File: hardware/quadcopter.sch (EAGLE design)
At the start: 60 parts, among them J1 AVR_SPI_PRG_6NS, J2 HEADER-4POS-2X2-0.1IN-FEMALE-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, J3 HEADER-10POSTH-254X10, J4 HEADER-4POS-2X2-0.1IN-FEMALE-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, Q3 MOSFET-FET-SI2302CDS-T1-E3CT-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, Q4 MOSFET-FET-SI2302CDS-T1-E3CT-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, Q5 MOSFET-FET-SI2302CDS-T1-E3CT-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, Q6 MOSFET-FET-SI2302CDS-T1-E3CT-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, U1 ATMEGA128RFA1, U2 IMU-LSM6DSOXTR-497-18367-1-ND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

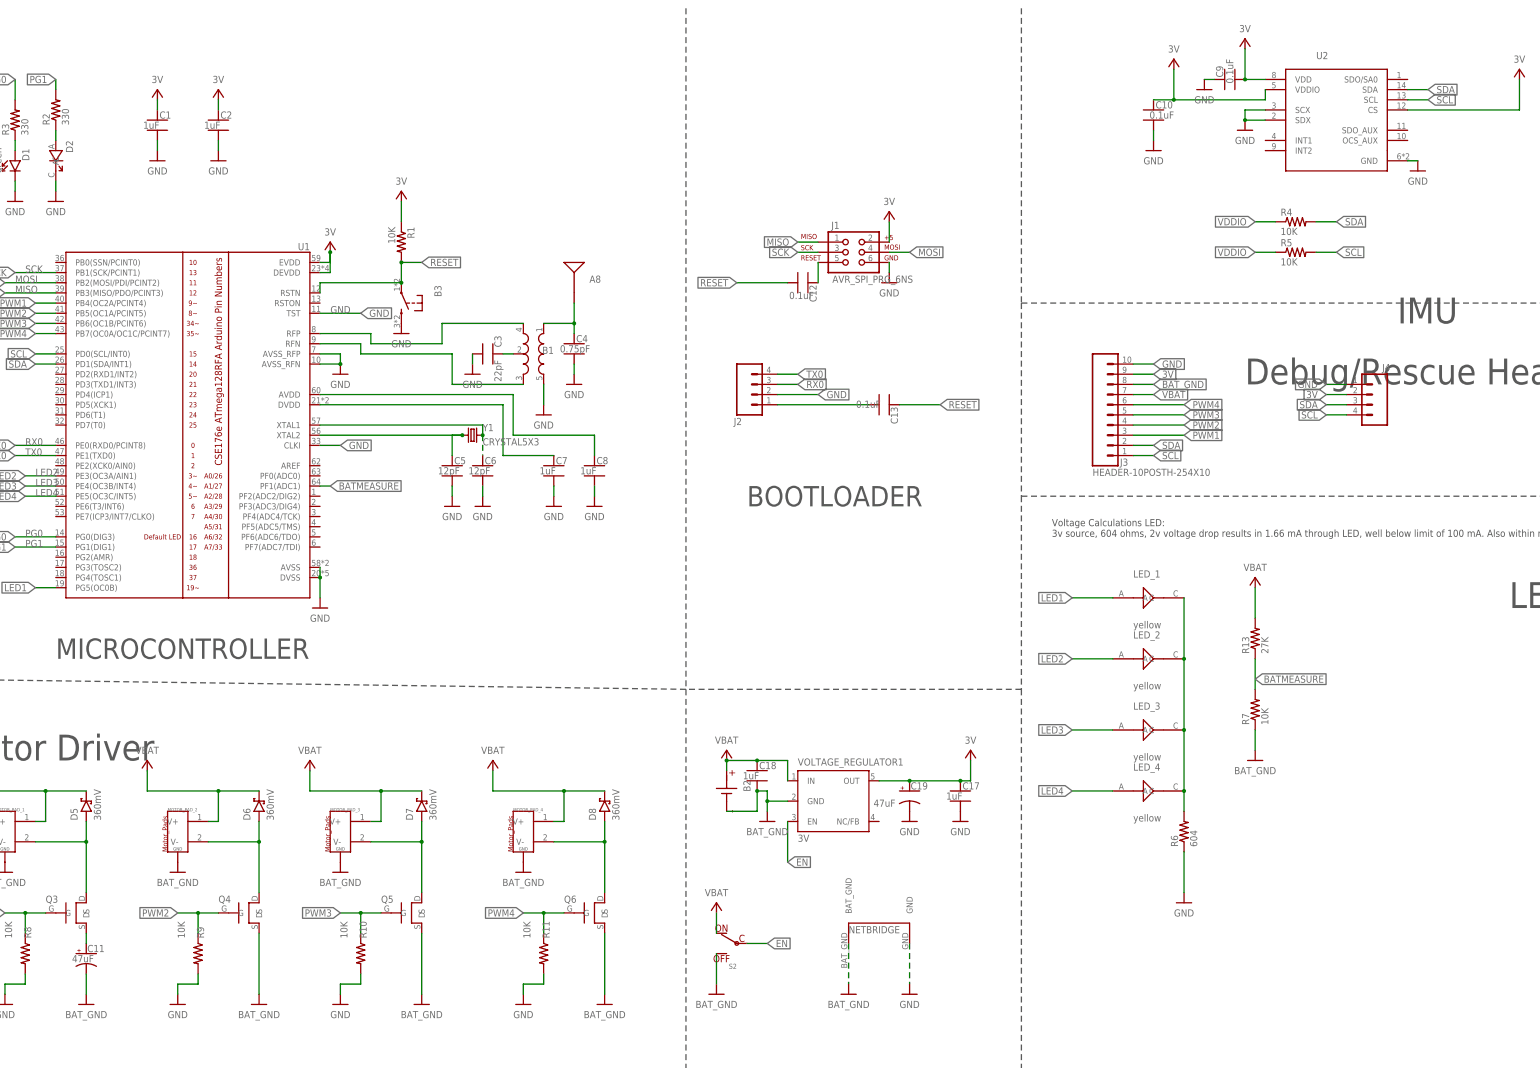
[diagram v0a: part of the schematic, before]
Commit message: fixing quadcopter schematic
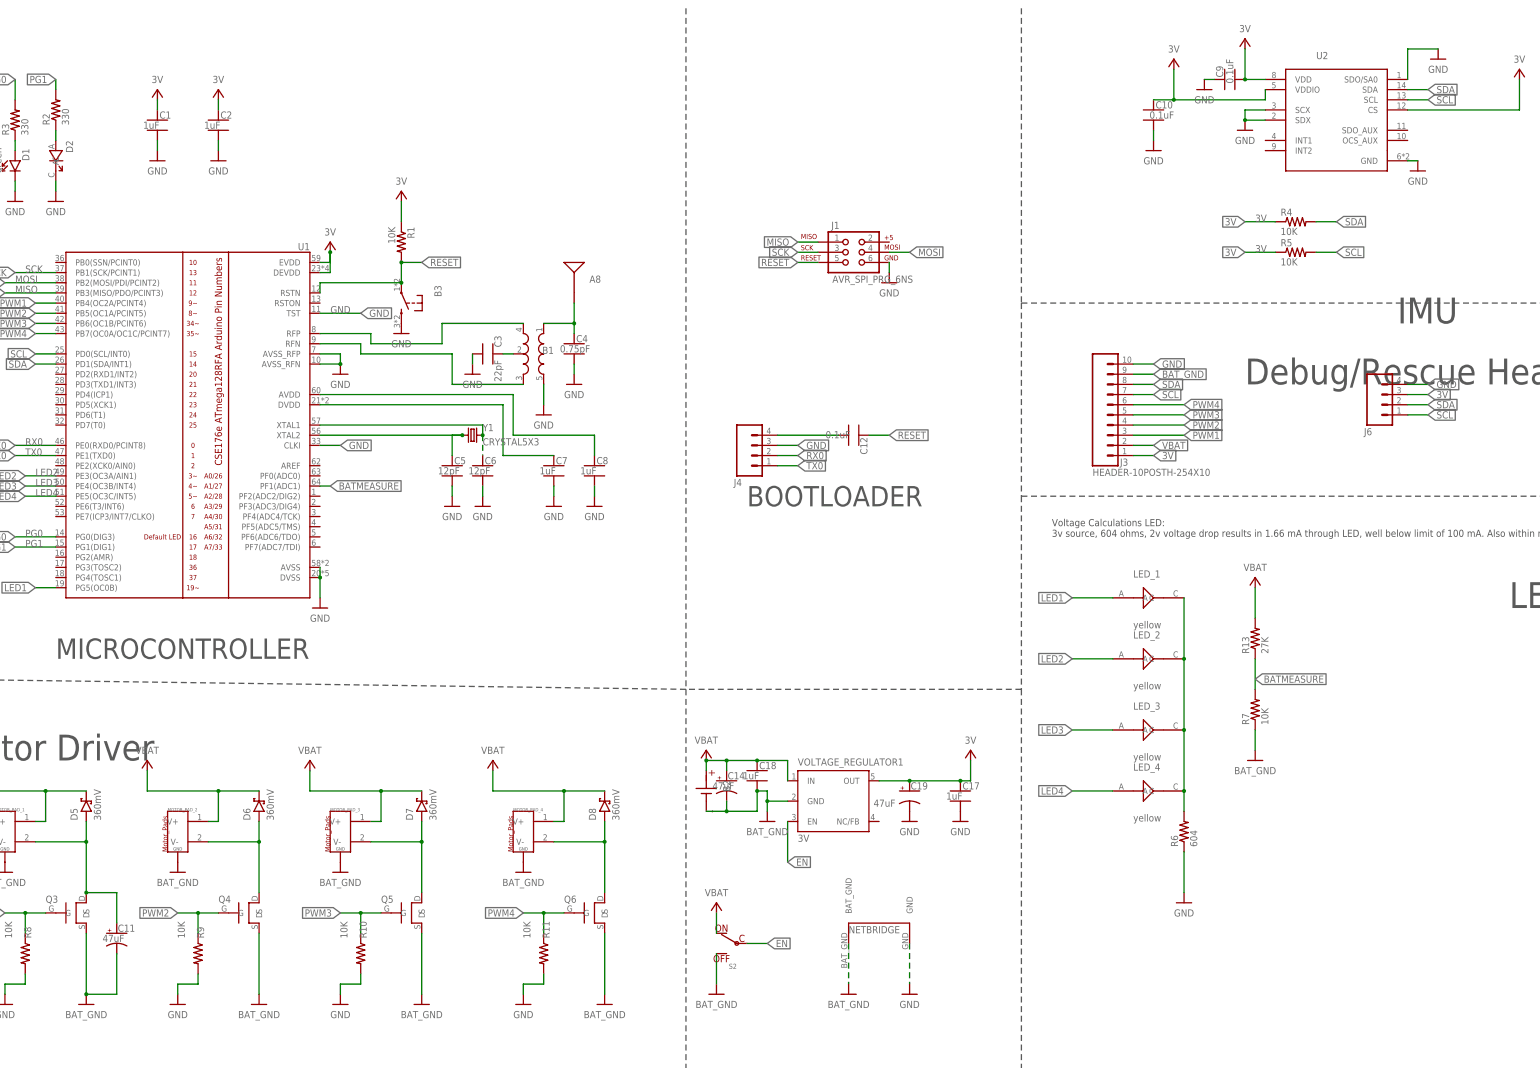
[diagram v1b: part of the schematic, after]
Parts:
- removed C13: 0.1uF, quadparts_prebuilt_2022:CAPACITOR-NP_SMD-2012-0805_CERAMIC-0.1UF
- removed J2: HEADER-4POS-2X2-0.1IN-FEMALE-SMD-BOTTOM-ENTRY, quadparts_prebuilt_2022:HEADER-4POS-2X2-0.1IN-FEMALE-SMD-BOTTOM-ENTRY
- added C14: 47uF, quadparts_prebuilt_2022:CAPACITOR-POL_47UF-SMD-1206-TAJA
- added J6: HEADER-4POS-0.1IN-FEMALE, quadparts_prebuilt_2022:HEADER-4POS-0.1IN-FEMALE
- J4: value HEADER-4POS-2X2-0.1IN-FEMALE-SMD-BOTTOM-ENTRY -> HEADER-4POS-0.1IN-FEMALE-SMD-BOTTOM-ENTRY; device quadparts_prebuilt_2022:HEADER-4POS-2X2-0.1IN-FEMALE-SMD-BOTTOM-ENTRY -> quadparts_prebuilt_2022:HEADER-4POS-0.1IN-FEMALE-SMD-BOTTOM-ENTRY
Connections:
- removed net N$15: C13.2, J2.1
- removed net N$16: C11.+, Q3.S
- removed net VDDIO: R4.1, R5.1
- net 3V: now also J3.1, J6.3, R4.1, R5.1; no longer J1.2, J3.9, J4.2
- net BAT_GND: now also C14.-, J3.9, Q3.S; no longer J3.8
- net GND: now also J4.3, J6.4, U2.SDO/SA0; no longer J2.2, J4.1
- net N$13: now also C12.2, J4.4; no longer C12.1, J1.5
- net N$18: now also C11.+
- net RESET: now also C12.1, J1.5; no longer C12.2, C13.1
- net RX0: now also J4.2; no longer J2.3
- net SCL: now also J3.7, J6.1; no longer J3.1, J4.4
- net SDA: now also J3.8, J6.2; no longer J3.2, J4.3
- net TX0: now also J4.1; no longer J2.4
- net VBAT: now also C14.+, J3.2; no longer J3.7
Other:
- moved on the sheet: B2, C11, C12, J4

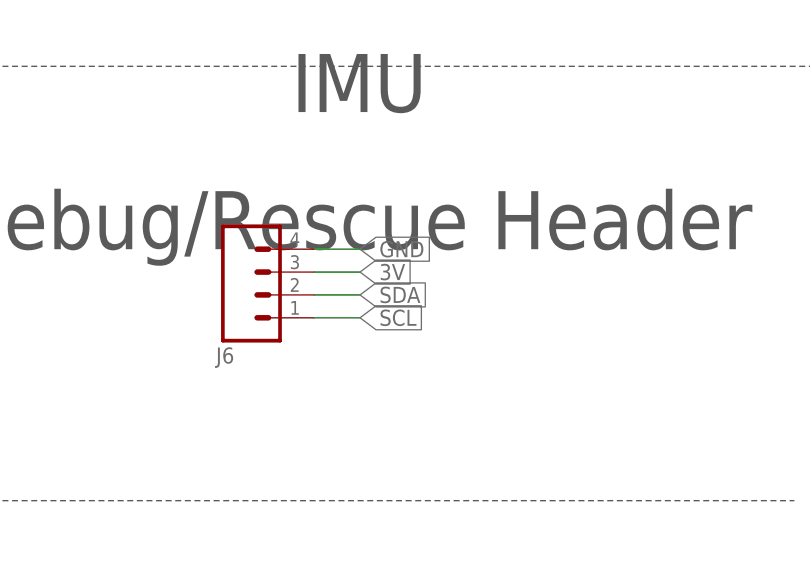
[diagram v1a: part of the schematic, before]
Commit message: fixing imu rescue header
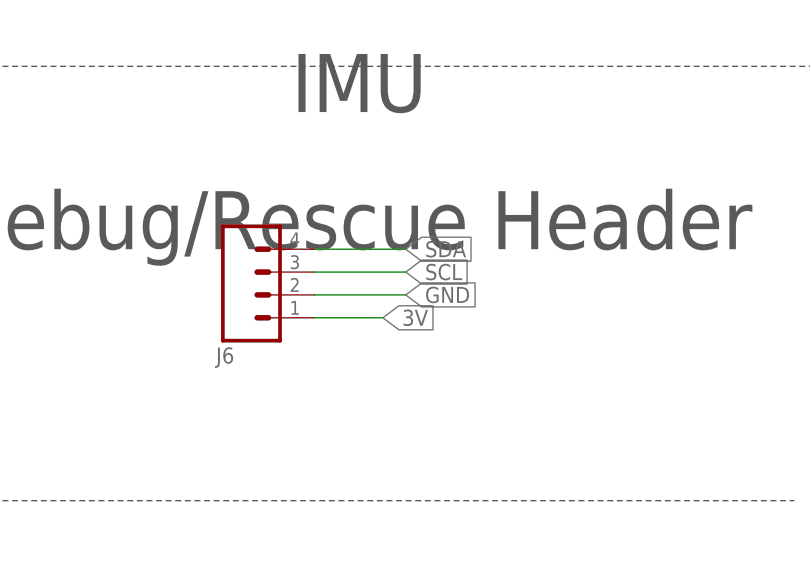
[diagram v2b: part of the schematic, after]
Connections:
- net 3V: now also J6.1; no longer J6.3
- net GND: now also J6.2; no longer J6.4
- net SCL: now also J6.3; no longer J6.1
- net SDA: now also J6.4; no longer J6.2
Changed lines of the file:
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@@
-</segment>
-<segment>
-<pinref part="J6" gate="G$1" pin="4"/>
-<wire x1="160.02" y1="50.8" x2="165.1" y2="50.8" width="0.1524" layer="91"/>
-<label x="165.1" y="50.8" size="1.778" layer="95" xref="yes"/>
 </segment>
 <segment>
@@
 <wire x1="2.54" y1="35.56" x2="7.62" y2="35.56" width="0.1524" layer="91"/>
 <label x="7.62" y="35.56" size="1.778" layer="95" xref="yes"/>
+</segment>
+<segment>
+<pinref part="J6" gate="G$1" pin="2"/>
+<wire x1="160.02" y1="45.72" x2="170.18" y2="45.72" width="0.1524" layer="91"/>
+<label x="170.18" y="45.72" size="1.778" layer="95" xref="yes"/>
 </segment>
 </net>
@@
 </segment>
 <segment>
-<pinref part="J6" gate="G$1" pin="3"/>
-<wire x1="160.02" y1="48.26" x2="165.1" y2="48.26" width="0.1524" layer="91"/>
-<label x="165.1" y="48.26" size="1.778" layer="95" xref="yes"/>
+<pinref part="J6" gate="G$1" pin="1"/>
+<wire x1="160.02" y1="43.18" x2="167.64" y2="43.18" width="0.1524" layer="91"/>
+<label x="167.64" y="43.18" size="1.778" layer="95" xref="yes"/>
 </segment>
 </net>
@@
 </segment>
 <segment>
-<pinref part="J6" gate="G$1" pin="2"/>
-<wire x1="160.02" y1="45.72" x2="165.1" y2="45.72" width="0.1524" layer="91"/>
-<label x="165.1" y="45.72" size="1.778" layer="95" xref="yes"/>
+<pinref part="J6" gate="G$1" pin="4"/>
+<wire x1="160.02" y1="50.8" x2="170.18" y2="50.8" width="0.1524" layer="91"/>
+<label x="170.18" y="50.8" size="1.778" layer="95" xref="yes"/>
 </segment>
 </net>
@@
 </segment>
 <segment>
-<pinref part="J6" gate="G$1" pin="1"/>
-<wire x1="160.02" y1="43.18" x2="165.1" y2="43.18" width="0.1524" layer="91"/>
-<label x="165.1" y="43.18" size="1.778" layer="95" xref="yes"/>
-</segment>
-</net>
+<pinref part="J6" gate="G$1" pin="3"/>
+<wire x1="160.02" y1="48.26" x2="170.18" y2="48.26" width="0.1524" layer="91"/>
+<label x="170.18" y="48.26" size="1.778" layer="95" xref="yes"/>
+</segment>
+</net>

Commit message: update schematic
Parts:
- added R12, R14, R15: 604, quadparts_prebuilt_2022:RESISTOR_SMD-2012-0805-604
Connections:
- net N$4 renamed RF_N
- net N$6 renamed RF_P
- new net N$14: LED_4.C, R6.2
- new net N$15: LED_2.C, R14.1
- new net N$16: LED_3.C, R12.2
- net GND: now also R12.1, R14.2, R15.1
- net N$12: now also R15.2; no longer LED_2.C, LED_3.C, LED_4.C, R6.2
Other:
- moved on the sheet: R13, R7

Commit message: fixing many issues from quick check
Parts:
- renumbered LED_1 to L1, LED_2 to L2, LED_3 to L3, LED_4 to L4, NETBRIDGE to NB, VOLTAGE_REGULATOR1 to VR1
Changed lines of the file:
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@@
 <part name="R7" library="quadparts_prebuilt_2022" deviceset="RESISTOR_" device="SMD-2012-0805-10K" value="10K"/>
 <part name="R13" library="quadparts_prebuilt_2022" deviceset="RESISTOR_" device="SMD-2012-0805-27K" value="27K"/>
-<part name="VOLTAGE_REGULATOR1" library="quadparts_prebuilt_2022" deviceset="TPS73633-DBVT" device="3V" value="3V"/>
+<part name="VR1" library="quadparts_prebuilt_2022" deviceset="TPS73633-DBVT" device="3V" value="3V"/>
 <part name="C17" library="quadparts_prebuilt_2022" deviceset="CAPACITOR-NP_" device="SMD-2012-0805_CERAMIC-1UF" value="1uF"/>
 <part name="C18" library="quadparts_prebuilt_2022" deviceset="CAPACITOR-NP_" device="SMD-2012-0805_CERAMIC-1UF" value="1uF"/>
@@
 <part name="GND43" library="quadparts_prebuilt_2022" deviceset="GND" device=""/>
 <part name="P+19" library="quadparts_prebuilt_2022" deviceset="3V" device=""/>
-<part name="NETBRIDGE" library="custom_v9" library_urn="urn:adsk.wipprod:fs.file:vf.hOpq96TzSi2cy5Li20AtXQ" deviceset="NETBRIDGE" device=""/>
+<part name="NB" library="custom_v9" library_urn="urn:adsk.wipprod:fs.file:vf.hOpq96TzSi2cy5Li20AtXQ" deviceset="NETBRIDGE" device=""/>
 <part name="GND17" library="quadparts_prebuilt_2022" deviceset="BAT_GND" device=""/>
 <part name="GND18" library="quadparts_prebuilt_2022" deviceset="GND" device=""/>
-<part name="LED_1" library="LED" deviceset="LED_YELLOW" device="" value="yellow"/>
-<part name="LED_2" library="LED" deviceset="LED_YELLOW" device="" value="yellow"/>
-<part name="LED_3" library="LED" deviceset="LED_YELLOW" device="" value="yellow"/>
-<part name="LED_4" library="LED" deviceset="LED_YELLOW" device="" value="yellow"/>
+<part name="L1" library="LED" deviceset="LED_YELLOW" device="" value="yellow"/>
+<part name="L2" library="LED" deviceset="LED_YELLOW" device="" value="yellow"/>
+<part name="L3" library="LED" deviceset="LED_YELLOW" device="" value="yellow"/>
+<part name="L4" library="LED" deviceset="LED_YELLOW" device="" value="yellow"/>
 <part name="B2" library="quadparts_prebuilt_2022" deviceset="BATTERY" device="-SCREW-TERMINAL"/>
 <part name="C14" library="quadparts_prebuilt_2022" deviceset="CAPACITOR-POL_" device="47UF-SMD-1206-TAJA" package3d_urn="urn:adsk.eagle:package:11793387/1" value="47uF"/>
@@
 <attribute name="NAME" x="171.2214" y="-19.05" size="1.778" layer="95" rot="R90"/>
 </instance>
-<instance part="VOLTAGE_REGULATOR1" gate="G$1" x="7.62" y="-60.96" smashed="yes">
+<instance part="VR1" gate="G$1" x="7.62" y="-60.96" smashed="yes">
 <attribute name="VALUE" x="7.62" y="-63.5" size="1.778" layer="96"/>
 <attribute name="NAME" x="7.62" y="-44.45" size="1.778" layer="95"/>
@@
 <attribute name="VALUE" x="50.8" y="-38.1" size="1.778" layer="96" rot="R180" align="center"/>
 </instance>
-<instance part="NETBRIDGE" gate="G$1" x="27.94" y="-86.36" smashed="yes">
+<instance part="NB" gate="G$1" x="27.94" y="-86.36" smashed="yes">
 <attribute name="NAME" x="20.32" y="-86.36" size="1.778" layer="95"/>
 </instance>
@@
 <attribute name="VALUE" x="35.56" y="-104.14" size="1.778" layer="96" align="center"/>
 </instance>
-<instance part="LED_1" gate="G$1" x="93.98" y="-2.54" smashed="yes">
+<instance part="L1" gate="G$1" x="93.98" y="-2.54" smashed="yes">
 <attribute name="NAME" x="91.44" y="2.54" size="1.778" layer="95"/>
 <attribute name="VALUE" x="91.44" y="-10.16" size="1.778" layer="96"/>
 </instance>
-<instance part="LED_2" gate="G$1" x="93.98" y="-17.78" smashed="yes">
+<instance part="L2" gate="G$1" x="93.98" y="-17.78" smashed="yes">
 <attribute name="NAME" x="91.44" y="-12.7" size="1.778" layer="95"/>
 <attribute name="VALUE" x="91.44" y="-25.4" size="1.778" layer="96"/>
 </instance>
-<instance part="LED_3" gate="G$1" x="93.98" y="-35.56" smashed="yes">
+<instance part="L3" gate="G$1" x="93.98" y="-35.56" smashed="yes">
 <attribute name="NAME" x="91.44" y="-30.48" size="1.778" layer="95"/>
 <attribute name="VALUE" x="91.44" y="-43.18" size="1.778" layer="96"/>
 </instance>
-<instance part="LED_4" gate="G$1" x="93.98" y="-50.8" smashed="yes">
+<instance part="L4" gate="G$1" x="93.98" y="-50.8" smashed="yes">
 <attribute name="NAME" x="91.44" y="-45.72" size="1.778" layer="95"/>
 <attribute name="VALUE" x="91.44" y="-58.42" size="1.778" layer="96"/>
@@
 </segment>
 <segment>
-<pinref part="NETBRIDGE" gate="G$1" pin="GND"/>
+<pinref part="NB" gate="G$1" pin="GND"/>
 <wire x1="35.56" y1="-88.9" x2="35.56" y2="-99.06" width="0.1524" layer="91" style="longdash"/>
 <pinref part="GND18" gate="1" pin="GND"/>
@@
 <wire x1="50.8" y1="-43.18" x2="50.8" y2="-48.26" width="0.1524" layer="91"/>
 <wire x1="50.8" y1="-48.26" x2="48.26" y2="-48.26" width="0.1524" layer="91"/>
-<pinref part="VOLTAGE_REGULATOR1" gate="G$1" pin="OUT"/>
+<pinref part="VR1" gate="G$1" pin="OUT"/>
 <wire x1="48.26" y1="-48.26" x2="35.56" y2="-48.26" width="0.1524" layer="91"/>
 <junction x="48.26" y="-48.26"/>
@@
 <wire x1="86.36" y1="-17.78" x2="76.2" y2="-17.78" width="0.1524" layer="91"/>
 <label x="76.2" y="-17.78" size="1.778" layer="95" rot="MR0" xref="yes"/>
-<pinref part="LED_2" gate="G$1" pin="A"/>
+<pinref part="L2" gate="G$1" pin="A"/>
 </segment>
 </net>
@@
 <wire x1="86.36" y1="-35.56" x2="76.2" y2="-35.56" width="0.1524" layer="91"/>
 <label x="76.2" y="-35.56" size="1.778" layer="95" rot="MR0" xref="yes"/>
-<pinref part="LED_3" gate="G$1" pin="A"/>
+<pinref part="L3" gate="G$1" pin="A"/>
 </segment>
 </net>
@@
 <wire x1="86.36" y1="-50.8" x2="76.2" y2="-50.8" width="0.1524" layer="91"/>
 <label x="76.2" y="-50.8" size="1.778" layer="95" rot="MR0" xref="yes"/>
-<pinref part="LED_4" gate="G$1" pin="A"/>
+<pinref part="L4" gate="G$1" pin="A"/>
 </segment>
 </net>
@@
 </segment>
 <segment>
-<pinref part="VOLTAGE_REGULATOR1" gate="G$1" pin="IN"/>
+<pinref part="VR1" gate="G$1" pin="IN"/>
 <wire x1="5.08" y1="-48.26" x2="5.08" y2="-43.18" width="0.1524" layer="91"/>
 <wire x1="5.08" y1="-43.18" x2="-2.54" y2="-43.18" width="0.1524" layer="91"/>
@@
 <wire x1="0" y1="-53.34" x2="0" y2="-50.8" width="0.1524" layer="91"/>
 <wire x1="0" y1="-53.34" x2="5.08" y2="-53.34" width="0.1524" layer="91"/>
-<pinref part="VOLTAGE_REGULATOR1" gate="G$1" pin="GND"/>
+<pinref part="VR1" gate="G$1" pin="GND"/>
 <wire x1="0" y1="-50.8" x2="-2.54" y2="-50.8" width="0.1524" layer="91"/>
 <wire x1="-2.54" y1="-50.8" x2="-2.54" y2="-55.88" width="0.1524" layer="91"/>
@@
 </segment>
 <segment>
-<pinref part="NETBRIDGE" gate="G$1" pin="BAT_GND"/>
+<pinref part="NB" gate="G$1" pin="BAT_GND"/>
 <wire x1="20.32" y1="-88.9" x2="20.32" y2="-99.06" width="0.1524" layer="91" style="longdash"/>
 <pinref part="GND17" gate="1" pin="BAT_GND"/>
@@
 <wire x1="86.36" y1="-2.54" x2="76.2" y2="-2.54" width="0.1524" layer="91"/>
 <label x="76.2" y="-2.54" size="1.778" layer="95" rot="MR0" xref="yes"/>
-<pinref part="LED_1" gate="G$1" pin="A"/>
+<pinref part="L1" gate="G$1" pin="A"/>
 </segment>
 </net>
@@
 </segment>
 <segment>
-<pinref part="VOLTAGE_REGULATOR1" gate="G$1" pin="EN"/>
+<pinref part="VR1" gate="G$1" pin="EN"/>
 <wire x1="5.08" y1="-58.42" x2="5.08" y2="-68.58" width="0.1524" layer="91"/>
 <label x="5.08" y="-68.58" size="1.778" layer="95" xref="yes"/>
@@
 <segment>
 <wire x1="104.14" y1="-50.8" x2="104.14" y2="-55.88" width="0.1524" layer="91"/>
-<pinref part="LED_4" gate="G$1" pin="C"/>
+<pinref part="L4" gate="G$1" pin="C"/>
 <pinref part="R6" gate="G$1" pin="2"/>
 </segment>
@@
 <segment>
 <wire x1="104.14" y1="-2.54" x2="109.22" y2="-2.54" width="0.1524" layer="91"/>
-<pinref part="LED_1" gate="G$1" pin="C"/>
+<pinref part="L1" gate="G$1" pin="C"/>
 <pinref part="R15" gate="G$1" pin="2"/>
 </segment>
@@
 <segment>
 <wire x1="104.14" y1="-17.78" x2="109.22" y2="-17.78" width="0.1524" layer="91"/>
-<pinref part="LED_2" gate="G$1" pin="C"/>
+<pinref part="L2" gate="G$1" pin="C"/>
 <pinref part="R14" gate="G$1" pin="1"/>
 </segment>
@@
 <segment>
 <wire x1="104.14" y1="-35.56" x2="109.22" y2="-35.56" width="0.1524" layer="91"/>
-<pinref part="LED_3" gate="G$1" pin="C"/>
+<pinref part="L3" gate="G$1" pin="C"/>
 <pinref part="R12" gate="G$1" pin="2"/>
 </segment>
